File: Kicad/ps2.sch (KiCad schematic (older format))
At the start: 1 part

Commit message: Completed Audio sheet.
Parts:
- gave numbers to parts that had none: 1
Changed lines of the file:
@@
 Sheet 7 9
 Title ""
-Date ""
+Date "2020-12-20"
 Rev ""
-Comp ""
-Comment1 ""
-Comment2 ""
+Comp "https://neotron-compute.github.io/"
+Comment1 "Licenced as CC BY-SA"
+Comment2 "Copyright (c) The Neotron Developers, 2020"
 Comment3 ""
 Comment4 ""
@@
 P 3550 3100
 AR Path="/5FDEE757" Ref="J?"  Part="1"
-AR Path="/5FDEDE75/5FDEE757" Ref="J?"  Part="1"
-F 0 "J?" H 3550 3798 50  0000 C CNN
+AR Path="/5FDEDE75/5FDEE757" Ref="J701"  Part="1"
+F 0 "J701" H 3550 3798 50  0000 C CNN
 F 1 "Double-mini-DIN-6" H 3550 3707 50  0000 C CNN
 F 2 "Neotron-Common-Hardware:Double_mini-DIN_6" H 3550 3350 50  0001 C CNN

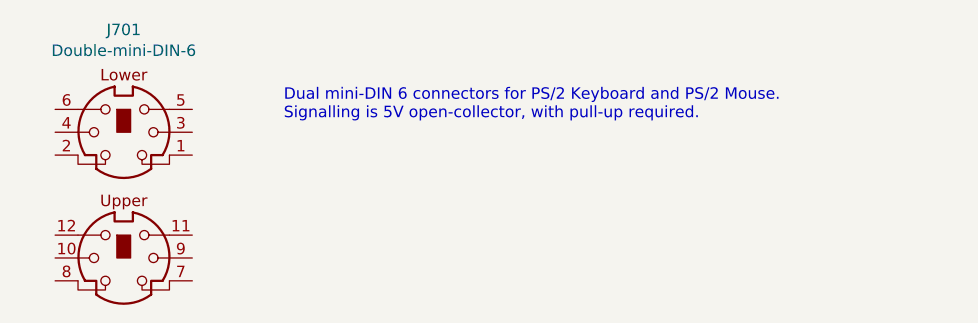
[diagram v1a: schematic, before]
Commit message: Brought in RS232 circuit from Neotron 32.
Also updated 3D models.
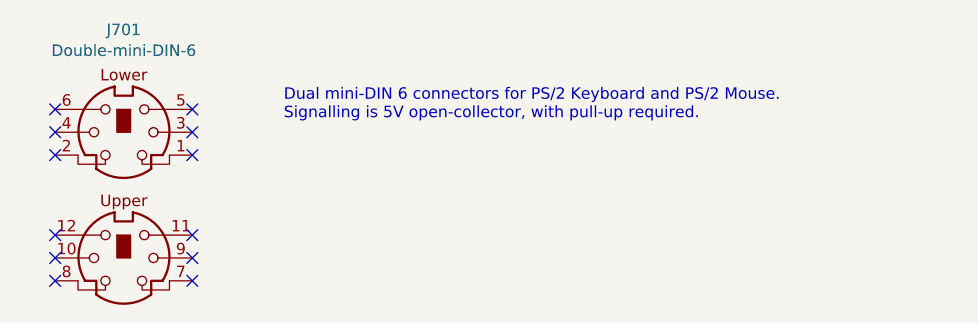
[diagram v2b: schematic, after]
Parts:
- J701: Digikey (none) -> 2092-KMDGX-6S/6S-S4N-ND
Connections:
- no-connect marks 0 -> 12
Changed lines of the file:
@@
 F 1 "Double-mini-DIN-6" H 3550 3707 50  0000 C CNN
 F 2 "Neotron-Common-Hardware:Double_mini-DIN_6" H 3550 3350 50  0001 C CNN
-F 3 "http://www.mouser.com/ds/2/18/40_c091_abd_e-75918.pdf" H 3550 3350 50  0001 C CNN
+F 3 "http://www.kycon.com/Pub_Eng_Draw/KMDGX-6S-6S-S4N.pdf" H 3550 3350 50  0001 C CNN
+F 4 "2092-KMDGX-6S/6S-S4N-ND" H 3550 3100 50  0001 C CNN "Digikey"
 	1    3550 3100
 	1    0    0    -1
@@
 Text Notes 4250 2800 0    50   ~ 0
 Dual mini-DIN 6 connectors for PS/2 Keyboard and PS/2 Mouse.\nSignalling is 5V open-collector, with pull-up required.
+NoConn ~ 3250 2750
+NoConn ~ 3250 2850
+NoConn ~ 3250 2950
+NoConn ~ 3250 3300
+NoConn ~ 3250 3400
+NoConn ~ 3250 3500
+NoConn ~ 3850 3500
+NoConn ~ 3850 3400
+NoConn ~ 3850 3300
+NoConn ~ 3850 2950
+NoConn ~ 3850 2850
+NoConn ~ 3850 2750
 $EndSCHEMATC

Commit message: Updating BOM with parts.
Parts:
- J701: DNP (none) -> 0
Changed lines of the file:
@@
 F 3 "http://www.kycon.com/Pub_Eng_Draw/KMDGX-6S-6S-S4N.pdf" H 3550 3350 50  0001 C CNN
 F 4 "2092-KMDGX-6S/6S-S4N-ND" H 3550 3100 50  0001 C CNN "Digikey"
+F 5 "0" H 3550 3100 50  0001 C CNN "DNP"
 	1    3550 3100
 	1    0    0    -1
